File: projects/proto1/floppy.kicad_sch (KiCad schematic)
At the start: 5 parts, among them J6 IDC_FDD, U22 PC8477BV

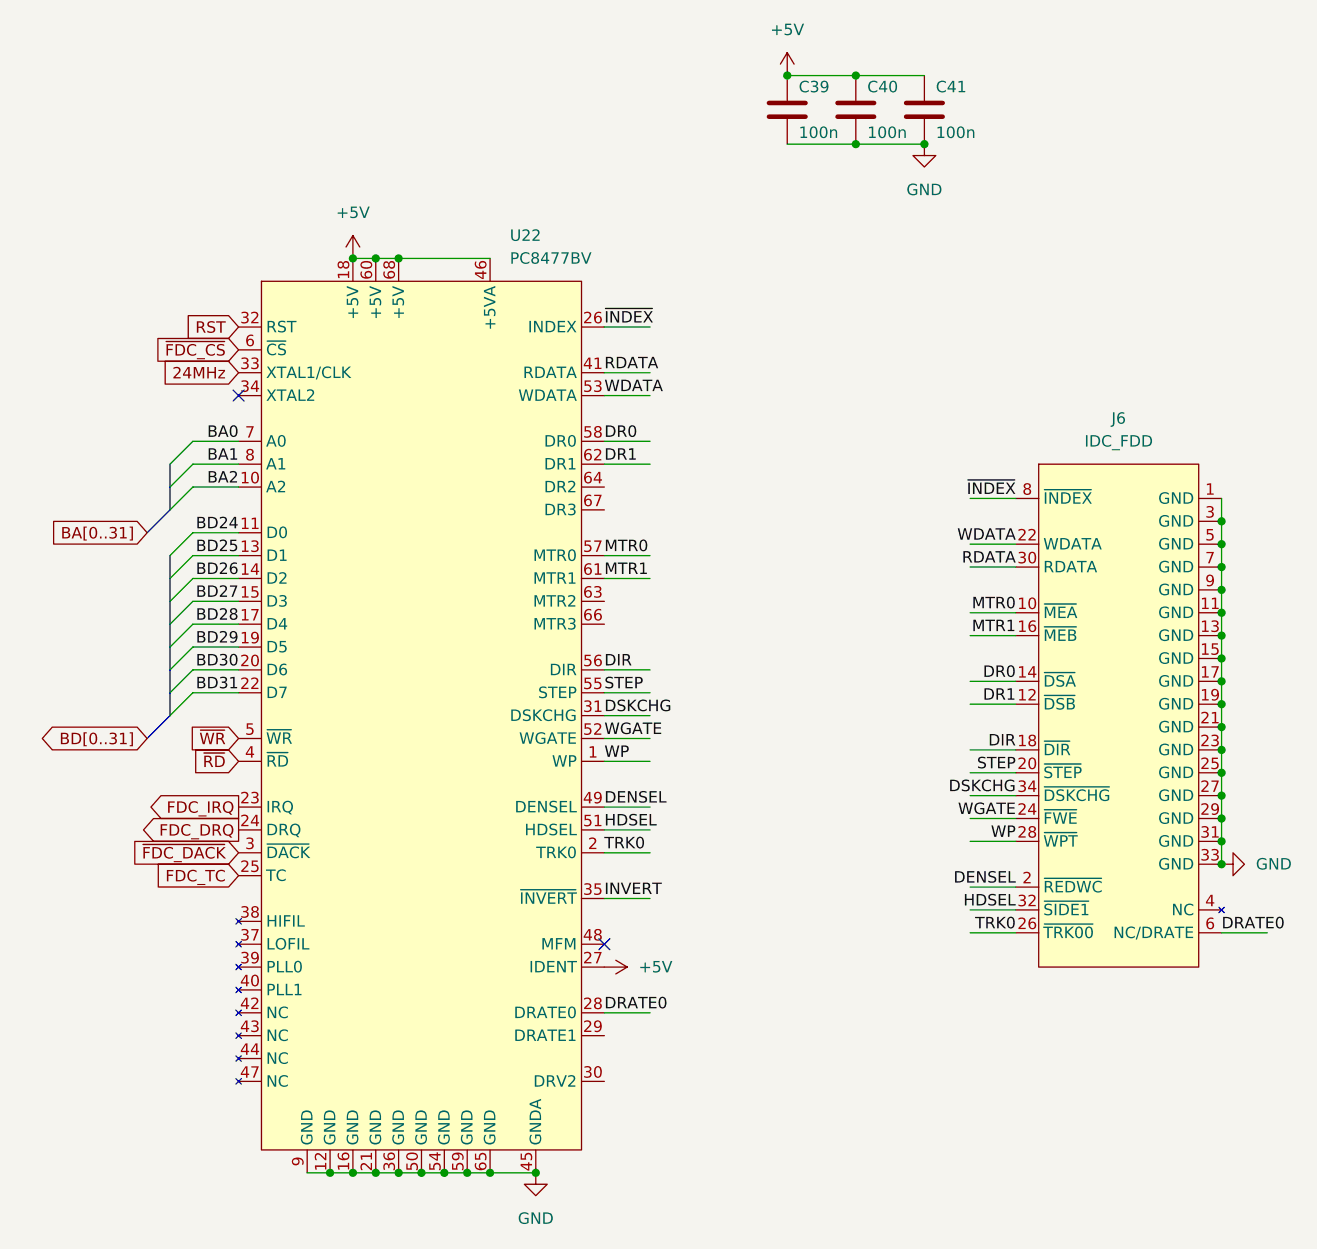
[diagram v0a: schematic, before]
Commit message: Renamed CMC to SCU, changed verification method to cocotb, and modified pcb schematic
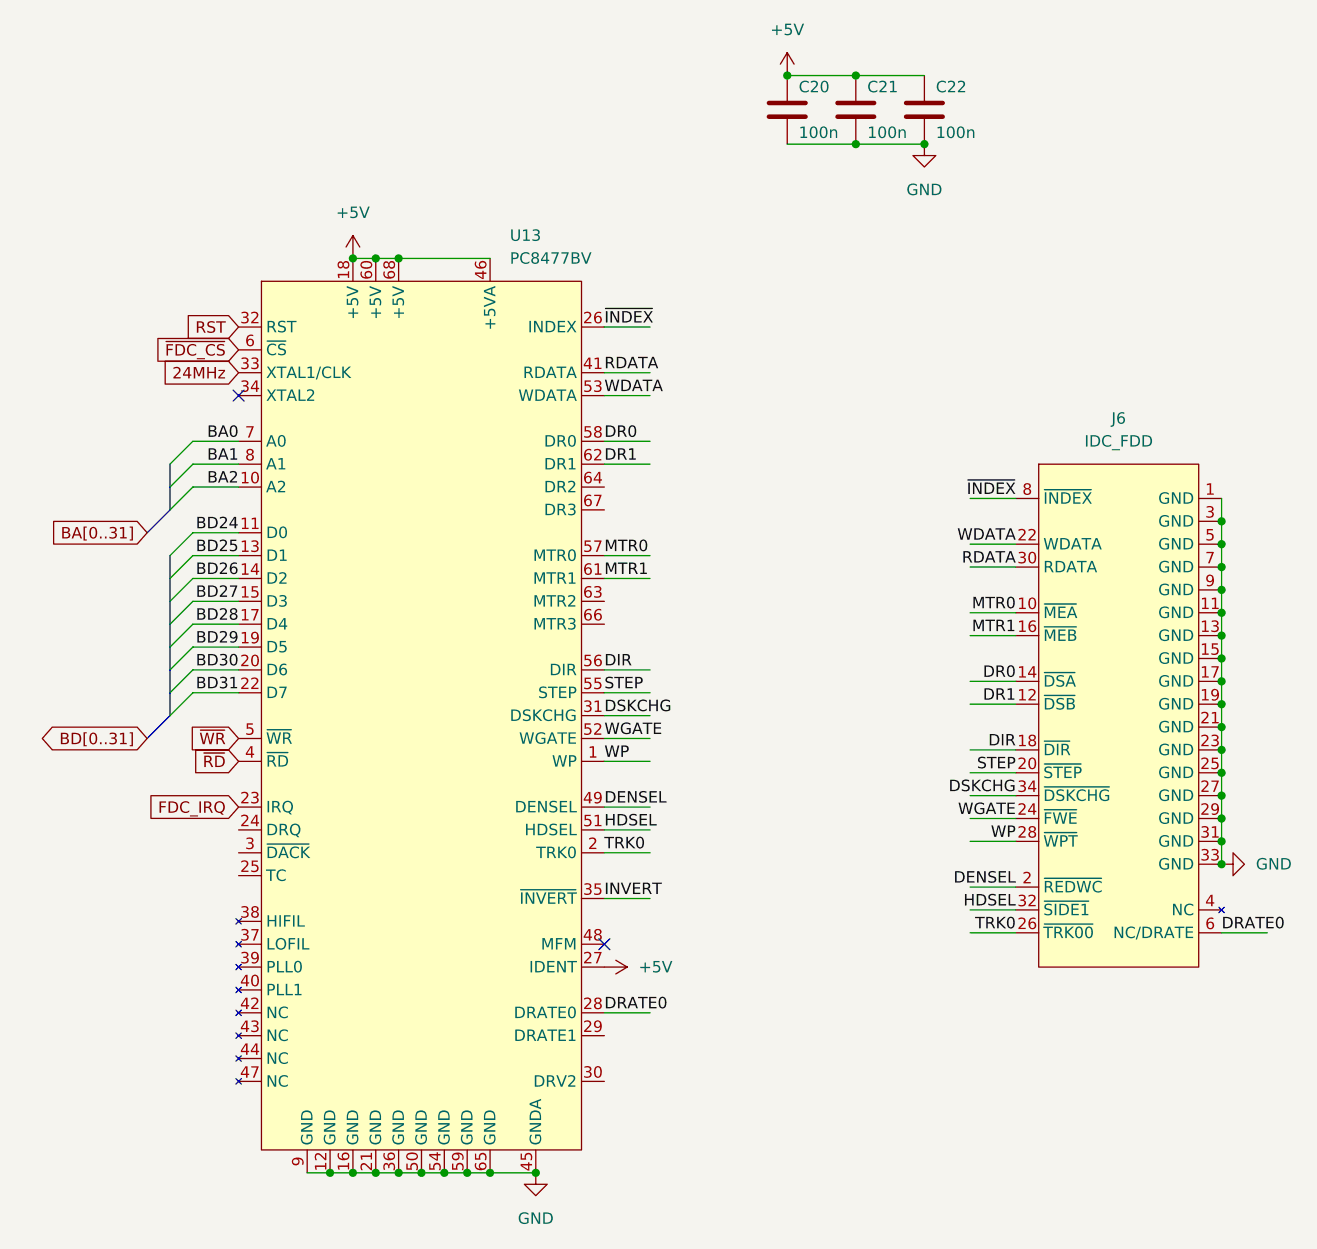
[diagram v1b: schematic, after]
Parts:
- renumbered C39 to C20, C40 to C21, C41 to C22, U22 to U13
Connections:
- net FDC_DRQ: no longer names the net of U13.24 (DRQ)
- net FDC_TC: no longer names the net of U13.25 (TC)
- net ~{FDC_DACK}: no longer names the net of U13.3 (~{DACK})
